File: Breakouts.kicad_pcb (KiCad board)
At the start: 2 copper layers, 189.9 x 66 mm, 13 parts, among them J1 Conn_01x08, J2 Conn_01x08, J3 Conn_01x08, J4 Conn_01x08, J5 Conn_02x04_Odd_Even, J6 Conn_01x06, J7 Conn_01x06, J8 AudioJack3, J9 Conn_01x03, K1 G5LE-1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

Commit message: big audio jack
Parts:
- added J10: AudioJack3_Switch, Connector_Audio:Jack_6.35mm_Neutrik_NMJ6HFD2_Horizontal, B.Cu at (209.1, 95.2)
- added J11: Conn_01x03, Connector_PinHeader_2.54mm:PinHeader_1x03_P2.54mm_Vertical_SMD_Pin1Left, B.Cu at (186.3, 94.9)
- added J12: Conn_01x03, Connector_PinHeader_2.54mm:PinHeader_1x03_P2.54mm_Vertical_SMD_Pin1Left, B.Cu at (186.3, 111.8)
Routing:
- net Net-(J12-Pin_1): track 0.00 -> 31.1 mm
- net Net-(J11-Pin_3): track 0.00 -> 30.5 mm
- net Net-(J11-Pin_2): track 0.00 -> 23.3 mm
- net Net-(J12-Pin_2): track 0.00 -> 23.3 mm
- net Net-(J12-Pin_3): track 0.00 -> 8.13 mm
- net Net-(J11-Pin_1): track 0.00 -> 8.10 mm
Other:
- board size 189.9 x 66 mm -> 189.9 x 96.5 mm

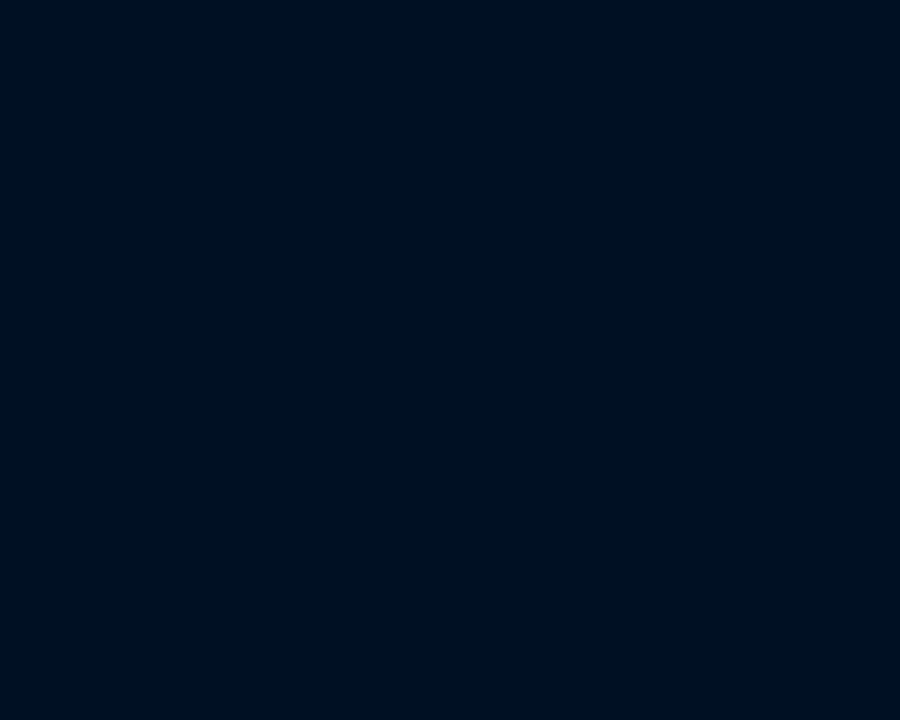
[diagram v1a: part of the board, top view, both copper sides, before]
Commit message: Add barrel jack
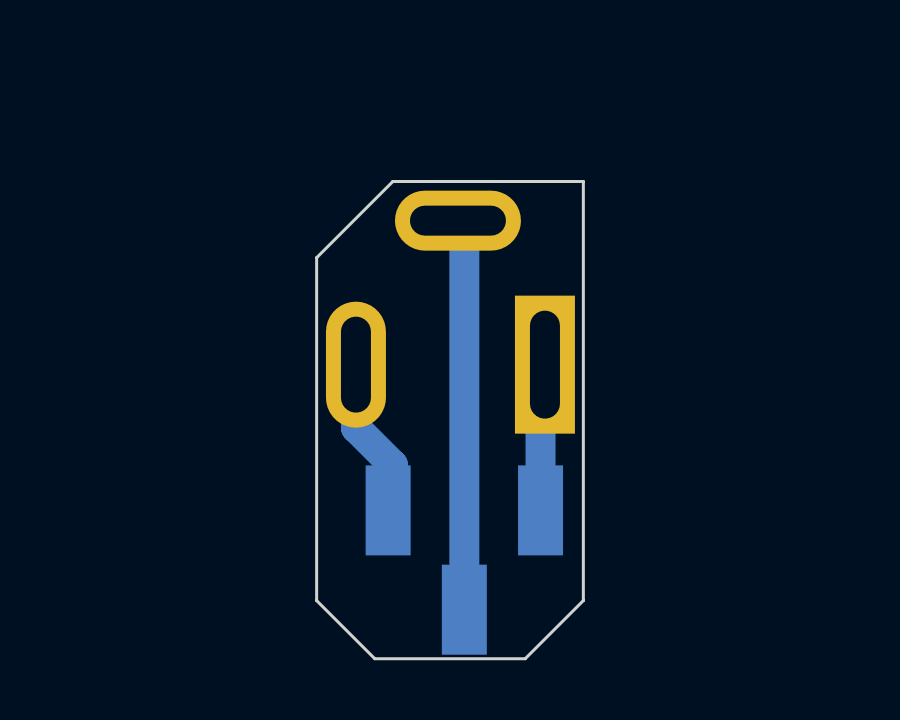
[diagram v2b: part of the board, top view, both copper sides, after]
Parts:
- added J13: Barrel_Jack_Switch, Connector_BarrelJack:BarrelJack_GCT_DCJ200-10-A_Horizontal, B.Cu at (256.5, 120.4)
- added J14: Conn_01x03, Connector_PinHeader_2.54mm:PinHeader_1x03_P2.54mm_Vertical_SMD_Pin1Left, B.Cu at (253.8, 126.9)
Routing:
- net Net-(J14-Pin_2): track 0.00 -> 13.1 mm
- net Net-(J14-Pin_1): track 0.00 -> 5.43 mm
- net Net-(J14-Pin_3): track 0.00 -> 4.92 mm
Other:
- board size 189.9 x 96.5 mm -> 189.9 x 111.2 mm

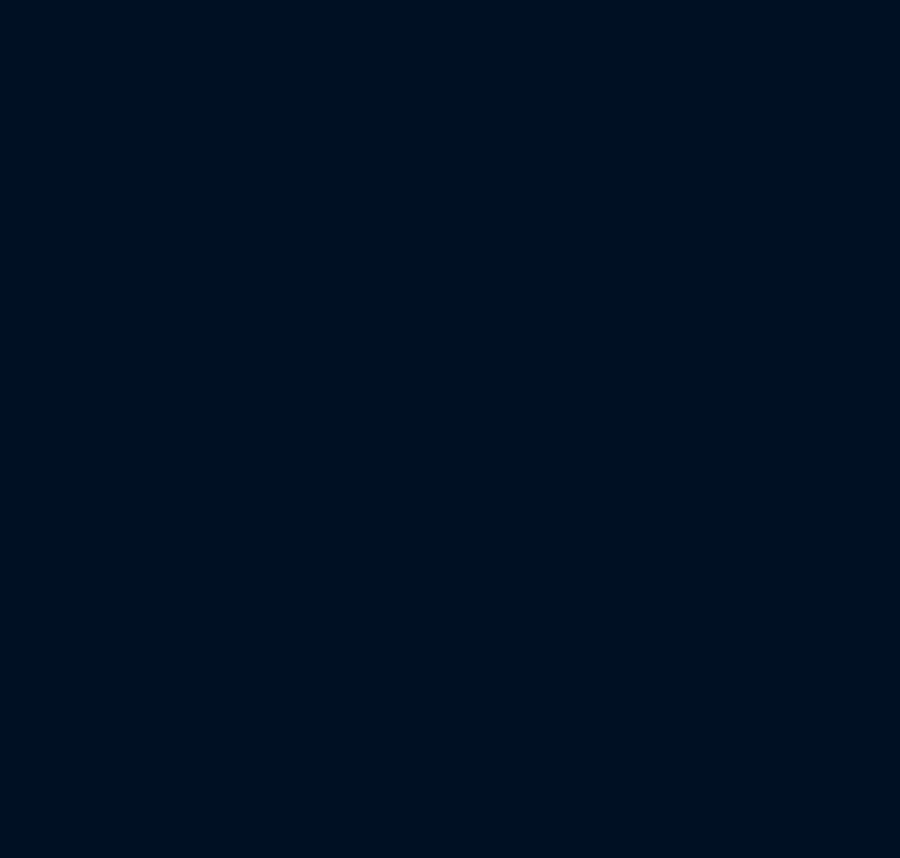
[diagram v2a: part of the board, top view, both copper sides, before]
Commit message: Add ULN2003 breakout
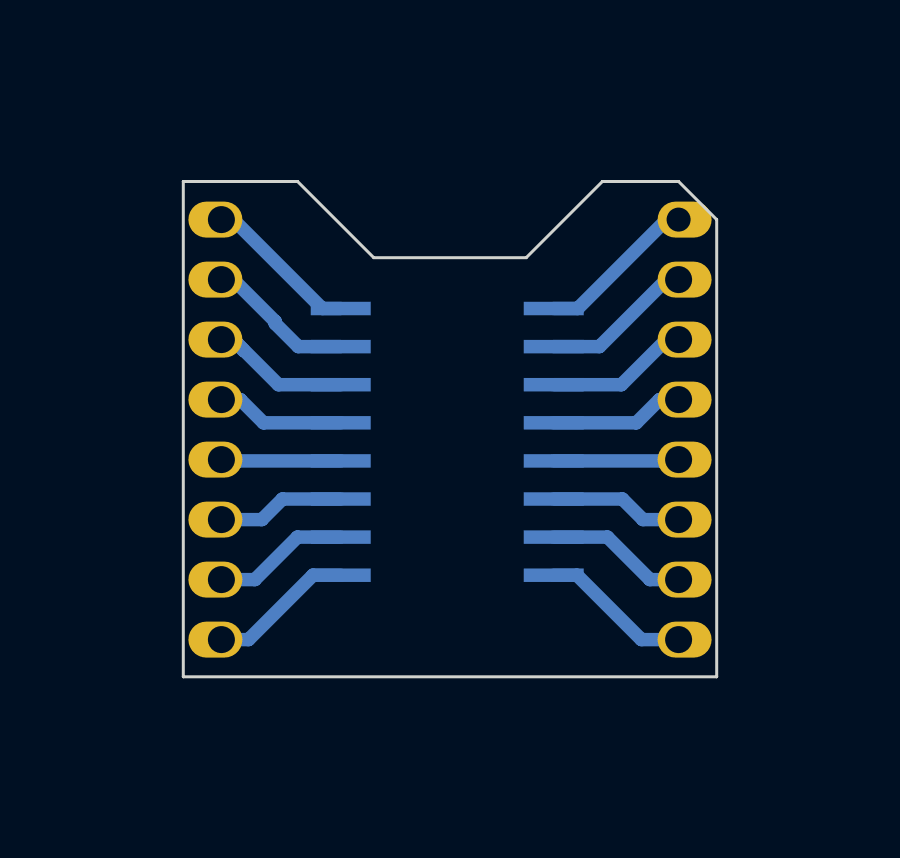
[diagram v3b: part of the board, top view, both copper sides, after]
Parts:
- added J15: Conn_01x08, Connector_PinHeader_2.00mm:PinHeader_1x08_P2.00mm_Vertical, B.Cu at (160.0, 88.9)
- added J16: Conn_01x08, Connector_PinHeader_2.00mm:PinHeader_1x08_P2.00mm_Vertical, B.Cu at (144.8, 88.9)
- added U4: ULN2003, Package_SO:SOIC-16W_5.3x10.2mm_P1.27mm, B.Cu at (152.3, 96.3)
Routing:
- net Net-(J16-Pin_3): track 0.00 -> 5.51 mm
- net Net-(J15-Pin_1): track 0.00 -> 5.39 mm
- net Net-(J16-Pin_1): track 0.00 -> 5.21 mm
- net Net-(J15-Pin_2): track 0.00 -> 5.09 mm
- net Net-(J15-Pin_8): track 0.00 -> 5.05 mm
- net Net-(J16-Pin_2): track 0.00 -> 4.94 mm
- net Net-(J16-Pin_8): track 0.00 -> 4.87 mm
- net Net-(J15-Pin_3): track 0.00 -> 4.79 mm
- net Net-(J15-Pin_7): track 0.00 -> 4.75 mm
- net Net-(J16-Pin_7): track 0.00 -> 4.56 mm
- net Net-(J15-Pin_4): track 0.00 -> 4.48 mm
- net Net-(J15-Pin_6): track 0.00 -> 4.45 mm
- net Net-(J16-Pin_4): track 0.00 -> 4.30 mm
- net Net-(J16-Pin_6): track 0.00 -> 4.26 mm
- net Net-(J15-Pin_5): track 0.00 -> 4.18 mm
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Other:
- outline, holes or cut-outs redrawn

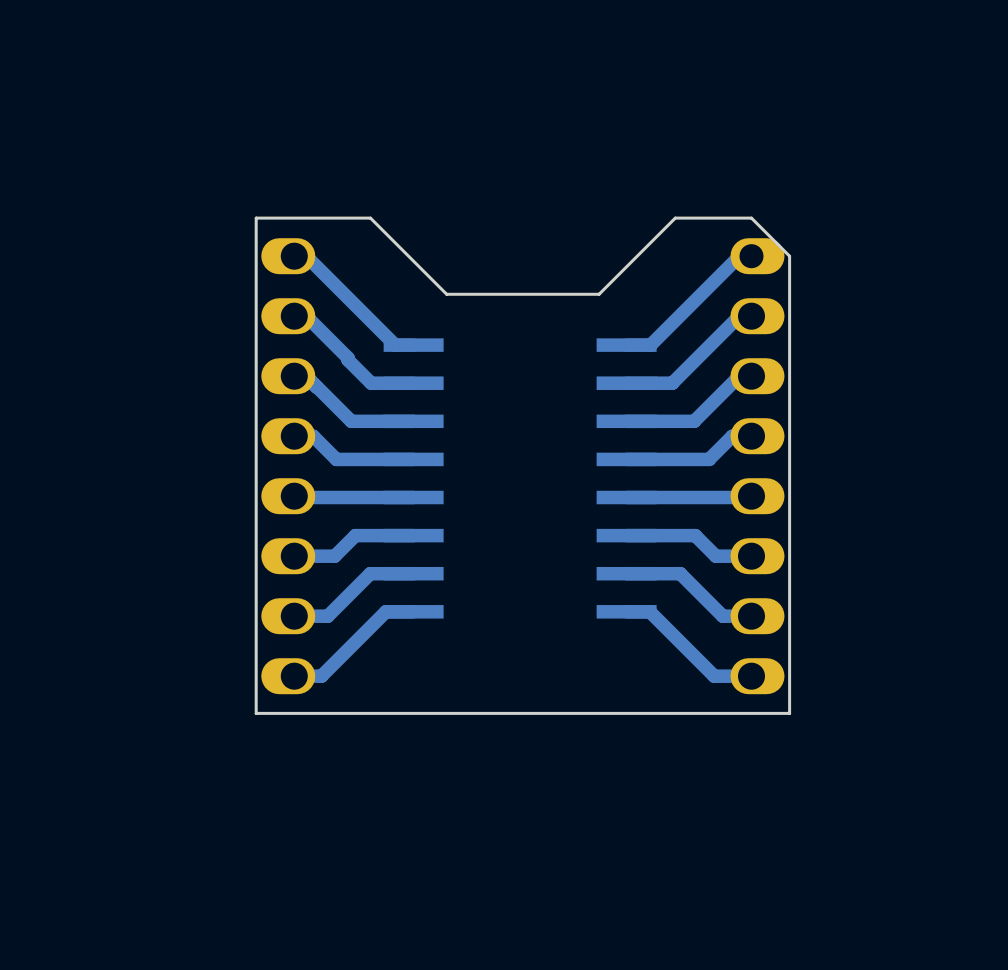
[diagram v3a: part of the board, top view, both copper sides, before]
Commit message: Add ULN2003 breakout with copper pour
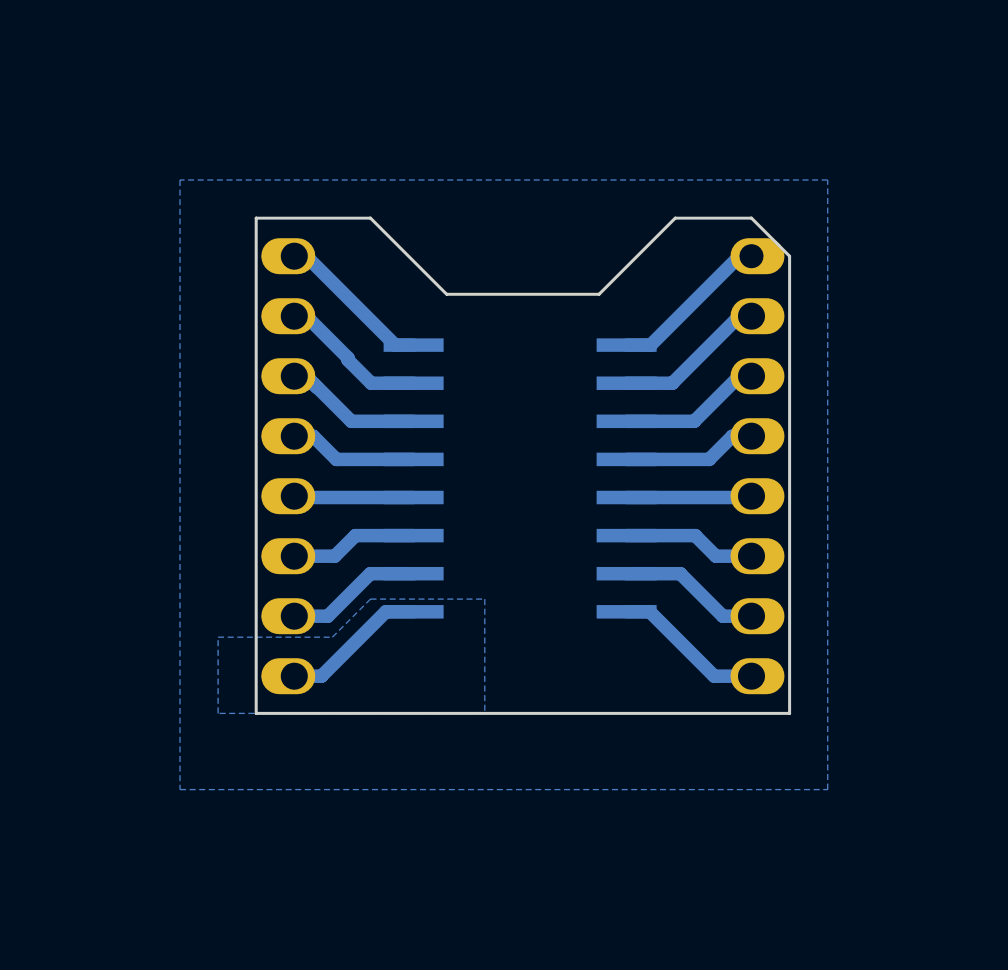
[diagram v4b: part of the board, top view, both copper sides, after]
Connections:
- net Net-(J16-Pin_8) renamed POWx
- J15 pad 8: Net-(J15-Pin_8) -> GND
- U4 pad 8: Net-(J15-Pin_8) -> GND
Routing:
- net Net-(J15-Pin_8): track 5.05 -> 0.00 mm
- net GND: track 5.91 -> 11.0 mm
- added copper zone on B.Cu, net POWx

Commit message: re-arrange pcbs
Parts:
- moved J6 88.7 mm to (186.0, 66.7)
- moved J7 88.7 mm to (186.0, 87.0)
- moved K1 88.7 mm to (200.2, 76.9)
- moved J5 84.8 mm to (169.7, 83.0)
- moved U2 84.8 mm to (167.4, 79.2)
- moved J8 75.2 mm to (172.4, 102.6)
- moved J9 75.2 mm to (167.7, 104.8)
- moved J14 62.7 mm to (194.2, 107.9)
- moved J13 62.7 mm to (196.8, 101.4)
- moved J10 55.3 mm to (153.8, 94.6)
- moved J11 55.3 mm to (131.0, 94.3)
- moved J12 55.3 mm to (131.0, 111.2)
- moved J3 43.0 mm to (152.4, 68.2)
- moved J4 43.0 mm to (129.5, 86.0)
- moved U1 43.0 mm to (141.0, 77.0)
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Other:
- board size 189.9 x 111.2 mm -> 107.3 x 49.5 mm

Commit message: Add FCC pos12 cable breakout
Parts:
- added J17: Flachband 12Pos, footprints:CONN12_1-1734742-2_TEC, B.Cu at (81.3, 136.1)
- added J18: Conn_01x06, Connector_PinHeader_2.54mm:PinHeader_1x06_P2.54mm_Vertical, B.Cu at (76.2, 139.7)
- added J19: Conn_01x06, Connector_PinHeader_2.54mm:PinHeader_1x06_P2.54mm_Vertical, B.Cu at (88.9, 139.7)
- added U3: ESP-12E, jlc_footprints:WIFIM-SMD_ESP-07, F.Cu at (13.1, 9.15)
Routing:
- net (no net): vias 0 -> 1
- added copper zone on B.Cu, net FFC_01
- added copper zone on B.Cu, net FFC_02
- added copper zone on B.Cu, net FFC_03
- added copper zone on B.Cu, net FFC_04
- added copper zone on B.Cu, net FFC_05
- added copper zone on B.Cu, net FFC_06
- added copper zone on B.Cu, net FFC_07
- added copper zone on B.Cu, net FFC_08
- added copper zone on B.Cu, net FFC_09
- added copper zone on B.Cu, net FFC_10
- added copper zone on B.Cu, net FFC_11
- added copper zone on B.Cu, net FFC_12
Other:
- board size 107.3 x 49.5 mm -> 130.1 x 76.8 mm

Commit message: Add TDA7575B Breakout
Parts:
- removed J19: Conn_01x06, Connector_PinHeader_2.54mm:PinHeader_1x06_P2.54mm_Vertical
- removed U999999: ESP-12E, ESP8266:ESP-12E
- added U5: TDA7575B, jlc_footprints:FLEXIWATT27-TH_27P-L29.3-W4.6-P1.00, B.Cu at (144.7, 144.2)
- J17: value Flachband 12Pos -> Conn_01x14; footprint footprints:CONN12_1-1734742-2_TEC -> Connector_PinHeader_2.54mm:PinHeader_1x14_P2.54mm_Vertical
- J18: value Conn_01x06 -> Conn_01x14; footprint Connector_PinHeader_2.54mm:PinHeader_1x06_P2.54mm_Vertical -> Connector_PinHeader_2.54mm:PinHeader_1x14_P2.54mm_Vertical
- moved J17 74.3 mm to (151.8, 159.4), turned to 0 degrees
- moved J18 64.7 mm to (137.8, 159.4)
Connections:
- J17 pad 1: FFC_01 -> Net-(J17-Pin_1)
- J17 pad 10: FFC_10 -> Net-(J17-Pin_10)
- J17 pad 11: FFC_11 -> Net-(J17-Pin_11)
- J17 pad 12: FFC_12 -> Net-(J17-Pin_12)
- J17 pad 13: unconnected-(J17-Pad13) -> Net-(J17-Pin_13)
- J17 pad 14: unconnected-(J17-Pad14) -> Net-(J17-Pin_14)
- J17 pad 2: FFC_02 -> Net-(J17-Pin_2)
- J17 pad 3: FFC_03 -> Net-(J17-Pin_3)
- J17 pad 4: FFC_04 -> Net-(J17-Pin_4)
- J17 pad 5: FFC_05 -> Net-(J17-Pin_5)
- J17 pad 6: FFC_06 -> Net-(J17-Pin_6)
- J17 pad 7: FFC_07 -> Net-(J17-Pin_7)
- J17 pad 8: FFC_08 -> Net-(J17-Pin_8)
- J17 pad 9: FFC_09 -> Net-(J17-Pin_9)
- J18 pad 1: FFC_01 -> Net-(J18-Pin_1)
- J18 pad 2: FFC_02 -> Net-(J18-Pin_2)
- J18 pad 3: FFC_03 -> Net-(J18-Pin_3)
- J18 pad 4: FFC_04 -> Net-(J18-Pin_4)
- J18 pad 5: FFC_05 -> Net-(J18-Pin_5)
- J18 pad 6: FFC_06 -> GND
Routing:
- net Net-(J18-Pin_13): track 0.00 -> 8.80 mm
- net Net-(J17-Pin_14): track 0.00 -> 7.71 mm
- net Net-(J17-Pin_13): track 0.00 -> 7.42 mm
- net Net-(J17-Pin_12): track 0.00 -> 6.78 mm
- net Net-(J17-Pin_11): track 0.00 -> 6.42 mm
- net Net-(J18-Pin_1): track 0.00 -> 6.20 mm
- net Net-(J17-Pin_10): track 0.00 -> 6.20 mm
- net Net-(J18-Pin_2): track 0.00 -> 6.20 mm
- net Net-(J18-Pin_12): track 0.00 -> 6.04 mm
- net Net-(J17-Pin_1): track 0.00 -> 5.98 mm
- net Net-(J17-Pin_9): track 0.00 -> 5.97 mm
- net Net-(J18-Pin_11): track 0.00 -> 5.82 mm
- net Net-(J18-Pin_3): track 0.00 -> 5.75 mm
- net Net-(J17-Pin_2): track 0.00 -> 5.75 mm
- net Net-(J17-Pin_8): track 0.00 -> 5.75 mm
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- added copper zone on B.Cu, net (none)
- removed copper zone on B.Cu, net FFC_01
- removed copper zone on B.Cu, net FFC_02
- removed copper zone on B.Cu, net FFC_03
- removed copper zone on B.Cu, net FFC_04
- removed copper zone on B.Cu, net FFC_05
- removed copper zone on B.Cu, net FFC_06
- removed copper zone on B.Cu, net FFC_07
- removed copper zone on B.Cu, net FFC_08
- removed copper zone on B.Cu, net FFC_09
- removed copper zone on B.Cu, net FFC_10
- removed copper zone on B.Cu, net FFC_11
- removed copper zone on B.Cu, net FFC_12
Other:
- board size 130.1 x 76.8 mm -> 130.1 x 95.9 mm

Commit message: Merge Flachband and TDA7575B
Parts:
- added J19: Flachband 12Pos, footprints:CONN12_1-1734742-2_TEC, B.Cu at (80.6, 156.2)
- added J20: Conn_01x06, Connector_PinHeader_2.54mm:PinHeader_1x06_P2.54mm_Vertical, B.Cu at (75.6, 159.9)
- added J21: Conn_01x06, Connector_PinHeader_2.54mm:PinHeader_1x06_P2.54mm_Vertical, B.Cu at (88.3, 159.9)
- J17: value Conn_01x14 -> Conn_01x1
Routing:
- added copper zone on B.Cu, net FFC_01
- added copper zone on B.Cu, net FFC_02
- added copper zone on B.Cu, net FFC_03
- added copper zone on B.Cu, net FFC_04
- added copper zone on B.Cu, net FFC_05
- added copper zone on B.Cu, net FFC_06
- added copper zone on B.Cu, net FFC_07
- added copper zone on B.Cu, net FFC_08
- added copper zone on B.Cu, net FFC_09
- added copper zone on B.Cu, net FFC_10
- added copper zone on B.Cu, net FFC_11
- added copper zone on B.Cu, net FFC_12
- removed copper zone on B.Cu, net (none)
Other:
- board size 130.1 x 95.9 mm -> 130.8 x 97 mm
